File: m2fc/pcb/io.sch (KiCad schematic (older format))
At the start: 30 parts, among them IC23 ADuM5201, IC24 ADuM5201, P7 CONN_4, P8 CONN_2, P9 CONN_4, U4 RG LED

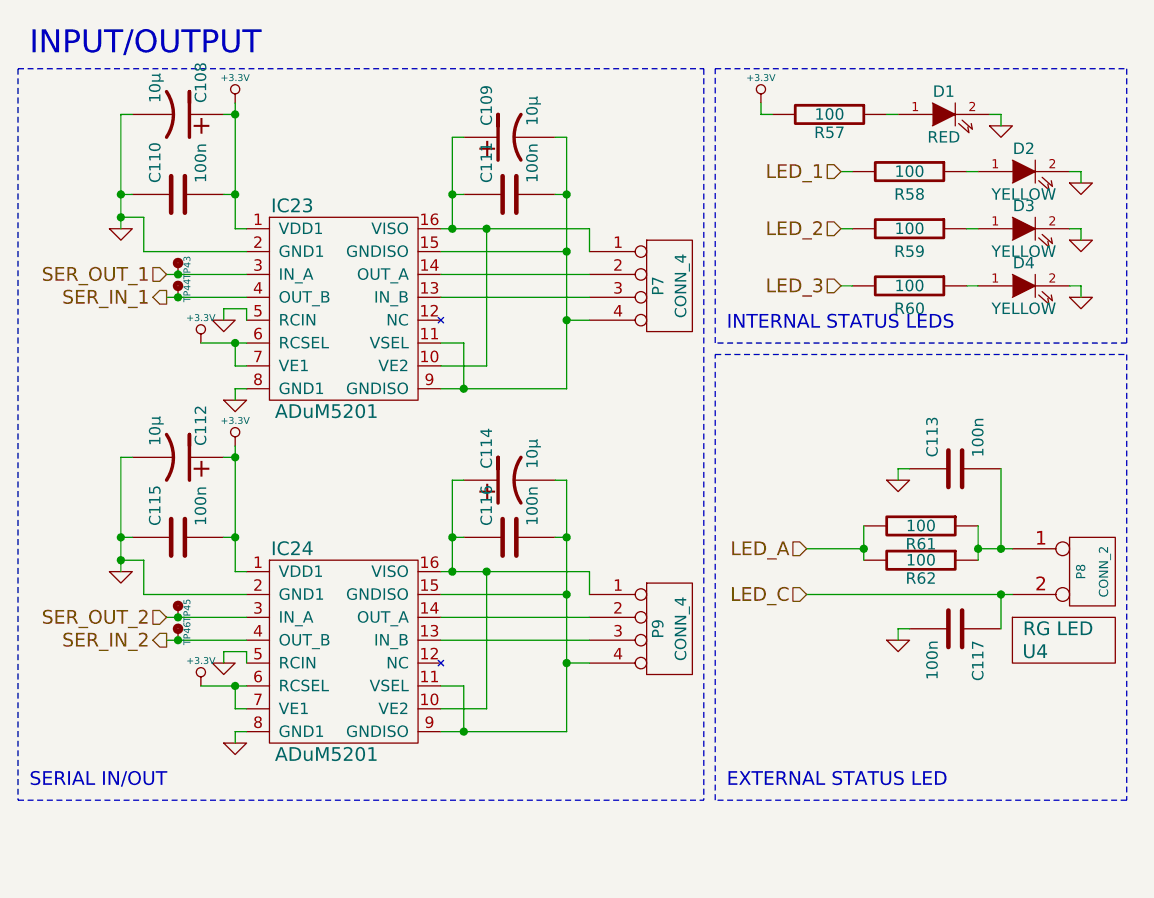
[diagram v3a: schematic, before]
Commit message: consistent layout/typography
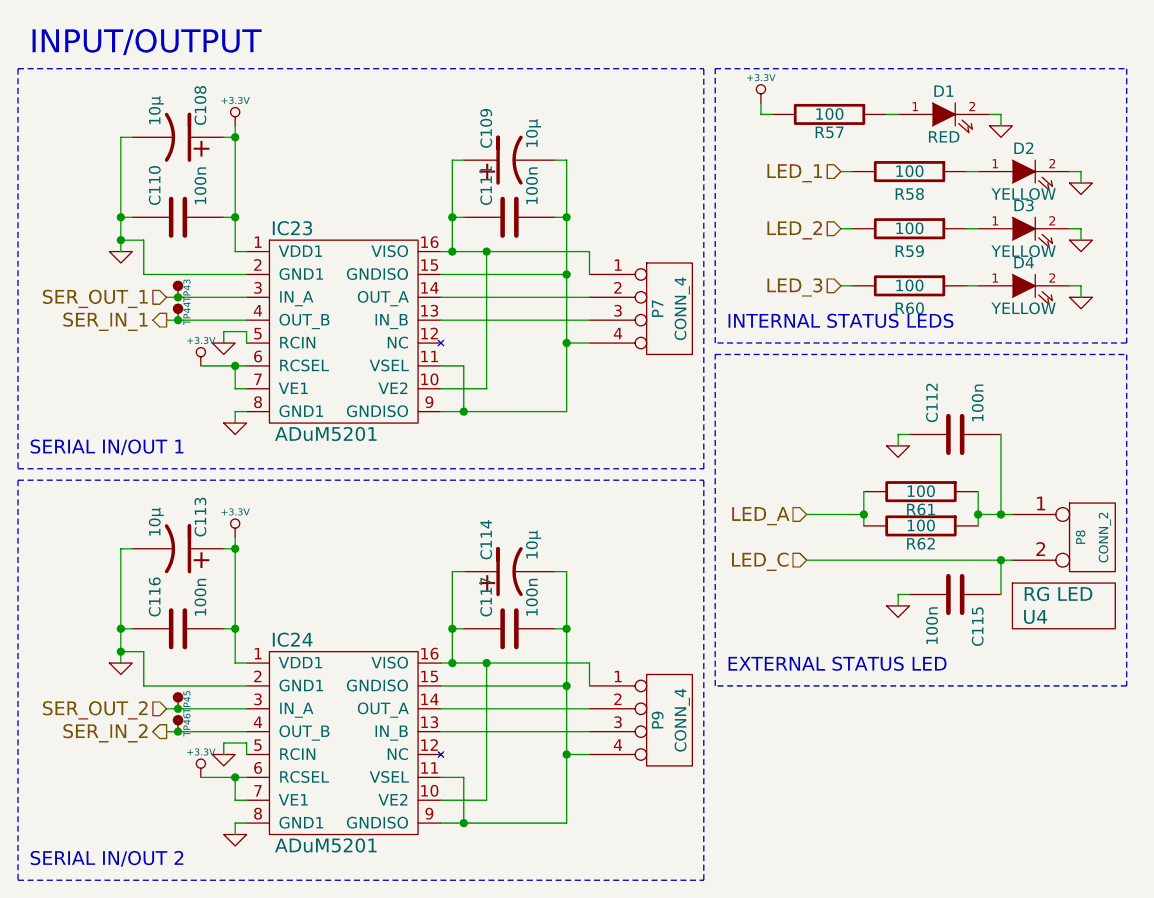
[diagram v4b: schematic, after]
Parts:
- removed C112: 10µ, 1411, symbol CP1
- removed C115: 100n, 0603, symbol C
- added C113: 10µ, 1411, symbol CP1
- added C117: 100n, 0603, symbol C
- renumbered C113 to C112, C117 to C115
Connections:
- net +3.3V: now also C116.2, C113.1
- net GND: now also C116.1, C113.2
- net at C114.1, IC24.10 (VE2), IC24.16 (VISO)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: now also C117.1; no longer C116.1
- net at C114.2, IC24.11 (VSEL), IC24.15 (GNDISO)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: now also C117.2; no longer C116.2
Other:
- note added: "SERIAL IN/OUT 1"
- note added: "SERIAL IN/OUT 2"
- note removed: "SERIAL IN/OUT"
- moved on the sheet: C108, C109, C110, C111, C112, C115, IC23, P7, P8, R61, R62, TP43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

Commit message: update m2fc sch with 3rd pyro and SJs
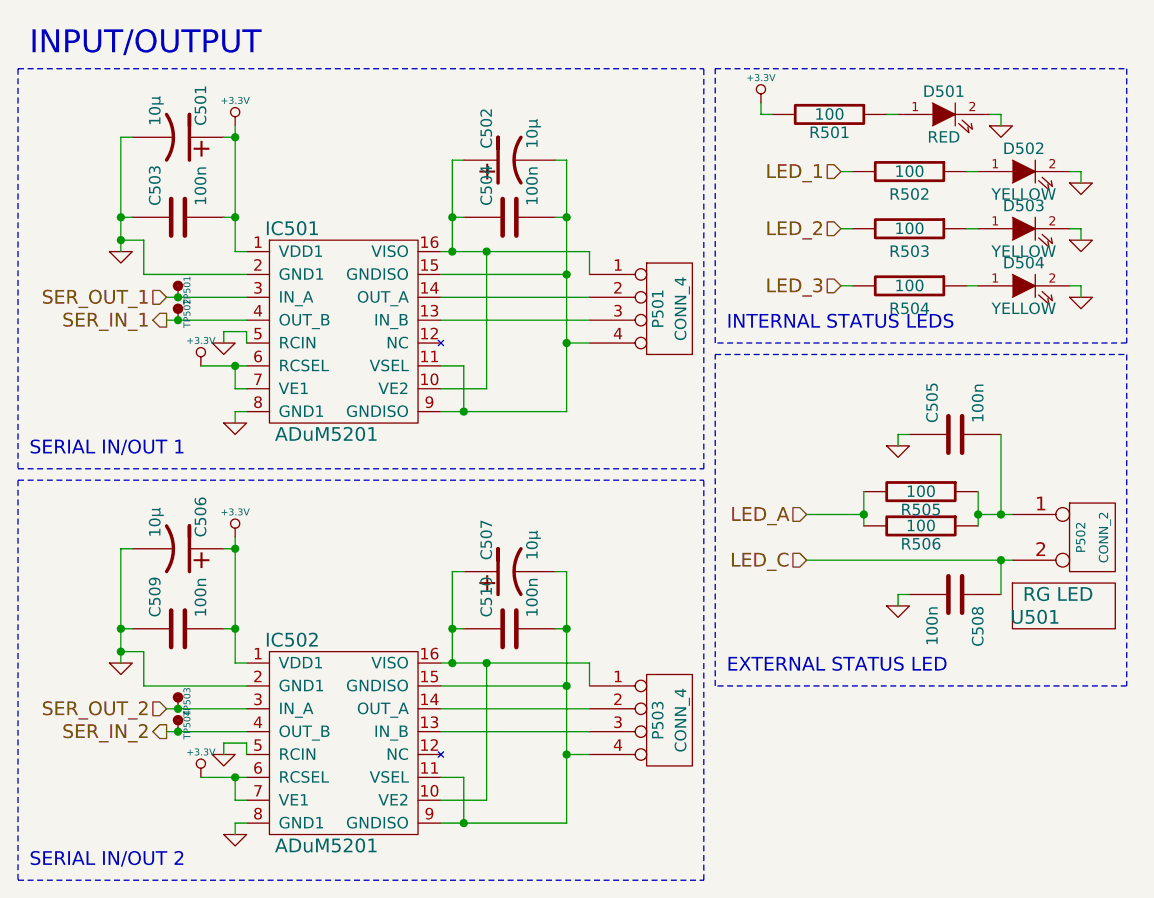
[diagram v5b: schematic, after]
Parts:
- renumbered C108 to C501, C109 to C502, C110 to C503, C111 to C504, C112 to C505, C113 to C506, C114 to C507, C115 to C508, C116 to C509, C117 to C510, D1 to D501, D2 to D502, D3 to D503, D4 to D504, IC23 to IC501, IC24 to IC502, P7 to P501, P8 to P502, P9 to P503, R57 to R501, R58 to R502, R59 to R503, R60 to R504, R61 to R505, R62 to R506, TP43 to TP501, TP44 to TP502, TP45 to TP503, TP46 to TP504, U4 to U501

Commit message: swap to JST PA range connectors
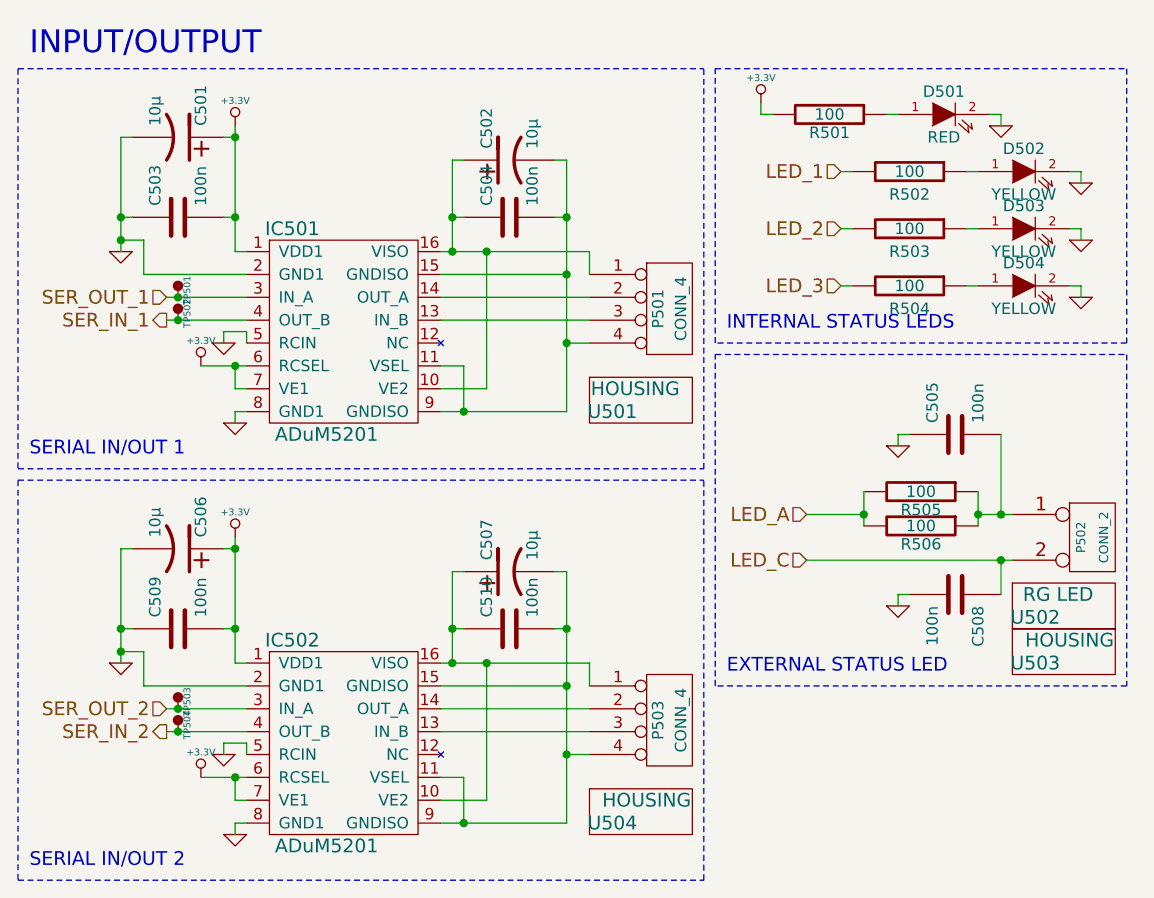
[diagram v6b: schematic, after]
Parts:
- added U501, U503, U504: HOUSING, symbol PART
- P501, P503: Farnell 1462920 -> (none); RS (none) -> 512-8484
- P502: Farnell 1462926 -> 1830747
- renumbered U501 to U502
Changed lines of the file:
@@
 F 2 "" H 6150 3350 60  0001 C CNN
 F 3 "" H 6150 3350 60  0001 C CNN
-F 4 "1462920" V 6150 3350 60  0001 C CNN "Farnell"
+F 4 "512-8484" V 6150 3350 60  0001 C CNN "RS"
 	1    6150 3350
 	1    0    0    -1
@@
 EXTERNAL STATUS LED
 $Comp
-L PART U501
+L PART U502
 U 1 1 53B6AD6D
 P 7700 4700
-F 0 "U501" H 7750 4700 60  0000 C CNN
+F 0 "U502" H 7750 4700 60  0000 C CNN
 F 1 "RG LED" H 7850 4800 60  0000 C CNN
 F 2 "" H 7700 4700 60  0001 C CNN
@@
 F 2 "" H 8000 4350 60  0000 C CNN
 F 3 "" H 8000 4350 60  0000 C CNN
-F 4 "1462926" H 8000 4350 60  0001 C CNN "Farnell"
+F 4 "1830747" H 8000 4350 60  0001 C CNN "Farnell"
 	1    8000 4350
 	1    0    0    -1
@@
 F 2 "" H 6150 5150 60  0001 C CNN
 F 3 "" H 6150 5150 60  0001 C CNN
-F 4 "1462920" V 6150 5150 60  0001 C CNN "Farnell"
+F 4 "512-8484" V 6150 5150 60  0001 C CNN "RS"
 	1    6150 5150
 	1    0    0    -1
@@
 Wire Notes Line
 	8150 3550 8150 5000
+$Comp
+L PART U503
+U 1 1 53CE2D27
+P 7700 4900
+F 0 "U503" H 7750 4900 60  0000 C CNN
+F 1 "HOUSING" H 7900 5000 60  0000 C CNN
+F 2 "" H 7700 4900 60  0000 C CNN
+F 3 "" H 7700 4900 60  0000 C CNN
+F 4 "1830726" H 7700 4900 60  0001 C CNN "Farnell"
+	1    7700 4900
+	1    0    0    -1
+$EndComp
+$Comp
+L PART U501
+U 1 1 53CE308B
+P 5850 3800
+F 0 "U501" H 5900 3800 60  0000 C CNN
+F 1 "HOUSING" H 6000 3900 60  0000 C CNN
+F 2 "" H 5850 3800 60  0000 C CNN
+F 3 "" H 5850 3800 60  0000 C CNN
+F 4 "1830729" H 5850 3800 60  0001 C CNN "Farnell"
+	1    5850 3800
+	1    0    0    -1
+$EndComp
+$Comp
+L PART U504
+U 1 1 53CE33FA
+P 5850 5600
+F 0 "U504" H 5900 5600 60  0000 C CNN
+F 1 "HOUSING" H 6050 5700 60  0000 C CNN
+F 2 "" H 5850 5600 60  0000 C CNN
+F 3 "" H 5850 5600 60  0000 C CNN
+F 4 "1830729" H 5850 5600 60  0001 C CNN "Farnell"
+	1    5850 5600
+	1    0    0    -1
+$EndComp
 $EndSCHEMATC

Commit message: sd pullups, shielded sgs
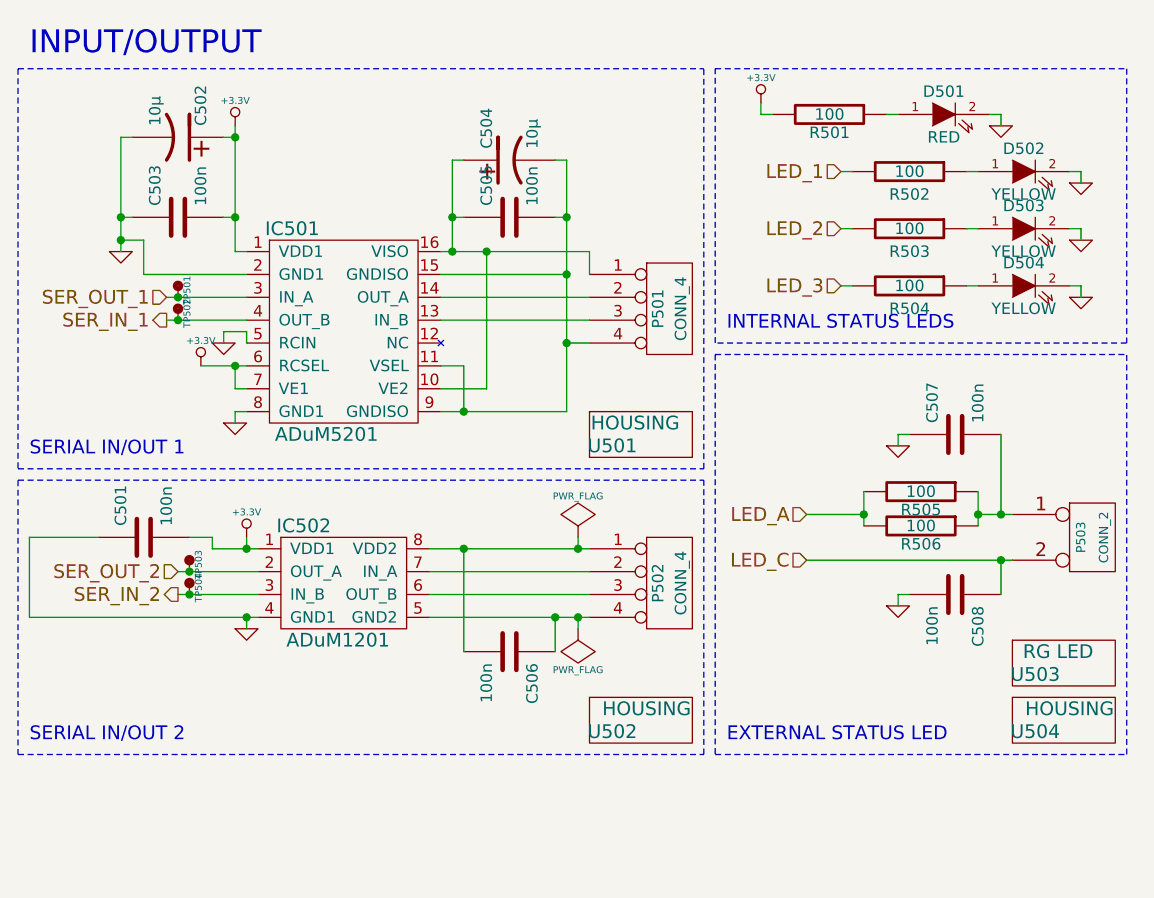
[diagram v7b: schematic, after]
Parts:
- removed C506, C507: 10µ, 1411, symbol CP1
- removed IC502: ADuM5201, symbol ADuM5201
- added IC502: ADuM1201, symbol ADuM1201
- C501: renamed from C509; footprint 0603 -> m2fc:C0603
- C503, C508: footprint 0603 -> m2fc:C0603
- C505: renamed from C504; footprint 0603 -> m2fc:C0603
- C506: renamed from C510; footprint 0603 -> m2fc:C0603
- C507: renamed from C505; footprint 0603 -> m2fc:C0603
- D501, D502, D503, D504: footprint 0603 -> m2fc:LED0603
- P501: footprint (none) -> m2fc:S04B-PASK-2
- P502: renamed from P503; footprint (none) -> m2fc:S04B-PASK-2
- P503: renamed from P502; footprint (none) -> m2fc:S02B-PASK-2
- R501, R502, R503, R504, R505, R506: footprint 0603 -> m2fc:R0603
- TP501, TP502, TP503, TP504: footprint (none) -> m2fc:TESTPAD
- renumbered C501 to C502, C502 to C504, U504 to U502, U502 to U503, U503 to U504
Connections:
- net +3.3V: now also IC502.1 (VDD1)
- net GND: now also IC502.4 (GND1)
- net SER_IN_2: now also IC502.3 (IN_B)
- net SER_OUT_2: now also IC502.2 (OUT_A)
- net at P502.1 (P1): now also C506.2, IC502.8 (VDD2); no longer C506.1
- net at P502.2 (P2): now also IC502.7 (IN_A)
- net at P502.3 (P3): now also IC502.6 (OUT_B)
- net at P502.4 (P4): now also C506.1, IC502.5 (GND2); no longer C506.2
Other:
- moved on the sheet: C501, C506, P502, TP503, TP504, U501, U502, U503, U504

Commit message: add esd diodes to m2fc
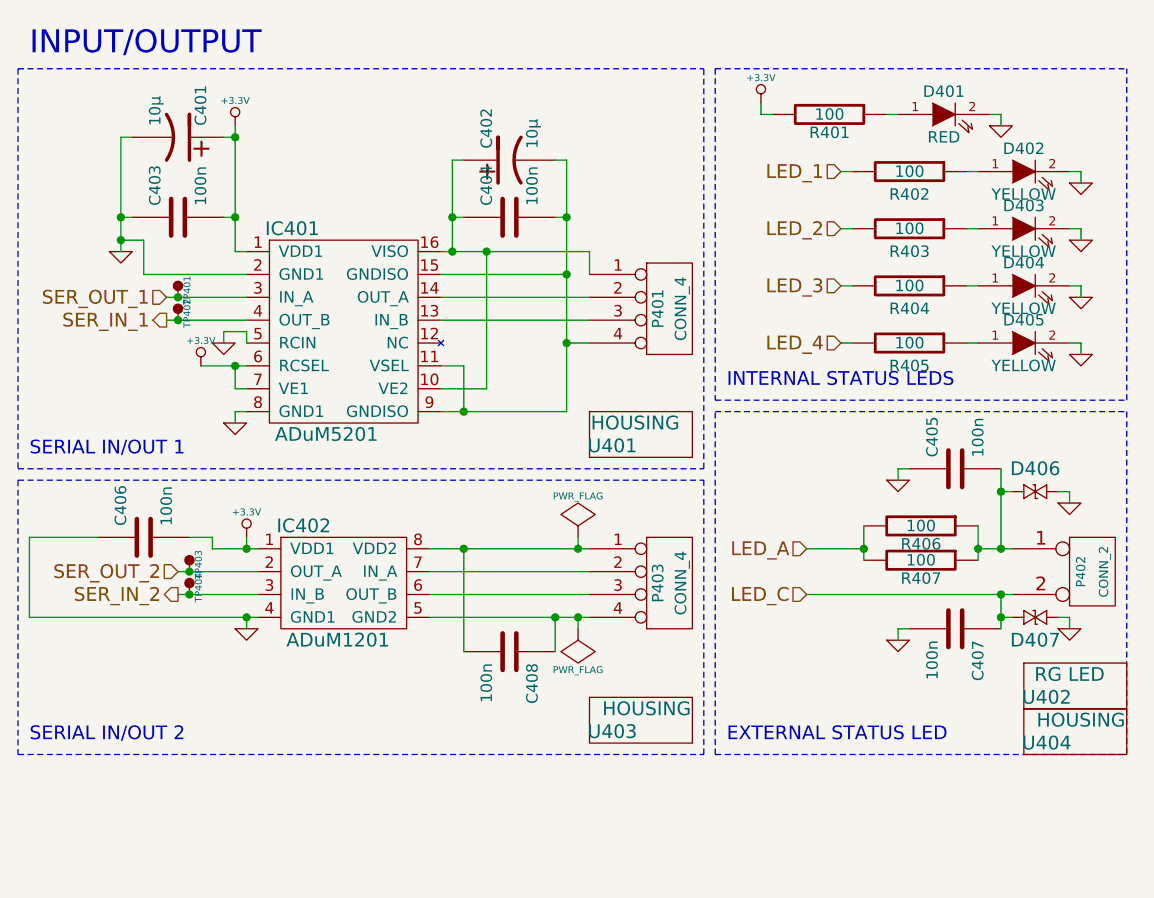
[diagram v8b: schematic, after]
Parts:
- added D405: YELLOW, m2fc:LED0603, symbol LED
- added D406, D407: CGA0402MLC-12G, m2fc:R0402, symbol CGA0402MLC-12G
- added R405: 100, m2fc:R0603, symbol R
- C401: renamed from C502; footprint 1411 -> m2fc:C0603; Farnell 2333026 -> 1657936
- C402: renamed from C504; footprint 1411 -> m2fc:C0603; Farnell 2333026 -> 1657936
- IC402: renamed from IC502; footprint (none) -> m2fc:SOIC8
- renumbered C503 to C403, C505 to C404, C507 to C405, C501 to C406, C508 to C407, C506 to C408, D501 to D401, D502 to D402, D503 to D403, D504 to D404, IC501 to IC401, P501 to P401, P503 to P402, P502 to P403, R501 to R401, R502 to R402, R503 to R403, R504 to R404, R505 to R406, R506 to R407, TP501 to TP401, TP502 to TP402, TP503 to TP403, TP504 to TP404, U501 to U401, U503 to U402, U502 to U403, U504 to U404
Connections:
- net GND: now also D405.2 (K), D406.1, D407.2
- net LED_C: now also D407.1
- net at C405.2, P402.1 (P1), R406.1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: now also D406.2
- new net: D405.1 (A), R405.1
- new net LED_4: R405.2
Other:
- moved on the sheet: C405, C407, P402, R406, R407, U402, U404
